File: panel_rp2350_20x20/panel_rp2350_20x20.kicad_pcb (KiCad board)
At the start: 6 copper layers, 45 x 45 mm, 548 parts, among them J1 Conn_01x04, J2 Conn_01x05, J3 Conn_01x05, J4 Conn_01x05, J5 Conn_01x05, SW1 SW_Push, SW2 SW_Push, U1 APS6404L-3SQR, U10 UCC27517, U11 UCC27517, U12 UCC27517, U13 UCC27517, U14 UCC27517, U15 UCC27517, U16 UCC27517, U17 UCC27517, U18 UCC27517, U19 UCC27517, U2 RP2354B_80QFN, U20 UCC27517, U21 UCC27517, U22 UCC27517, U23 UCC27517, U24 UCC27517, U25 UCC27517, U26 UCC27517, U27 UCC27517, U28 UCC27517, U29 UCC27517, U3 UCC27517, U30 UCC27517, U31 UCC27517, U32 UCC27517, U33 UCC27517, U34 UCC27517, U35 UCC27517, U36 UCC27517, U37 UCC27517, U38 UCC27517, U39 UCC27517, U4 UCC27517, U40 UCC27517, U41 UCC27517, U42 UCC27517, U43 AP2112K-3.3, U5 UCC27517, U6 UCC27517, U7 UCC27517, U8 UCC27517, U9 UCC27517, Y1 ABM8-272-T3

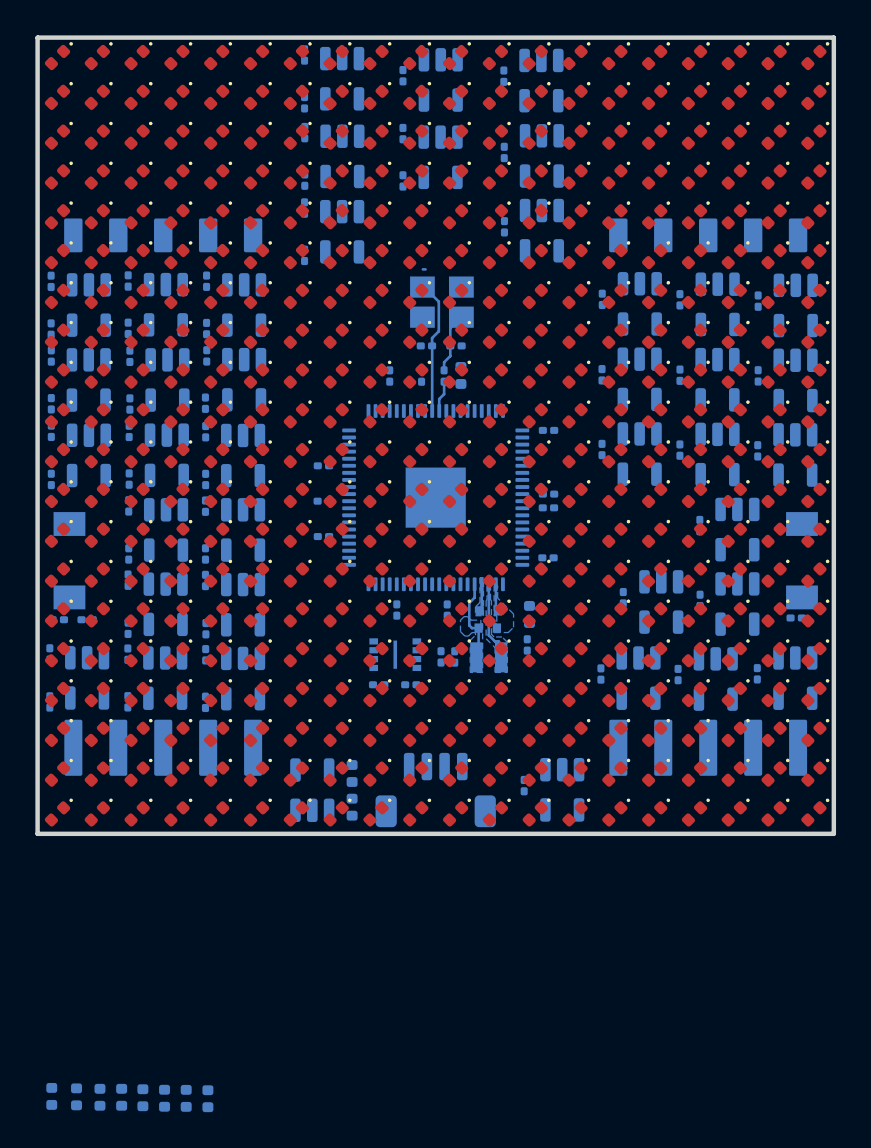
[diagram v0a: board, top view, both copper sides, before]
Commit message: Work on layout for rp2350 20x20 array panels.
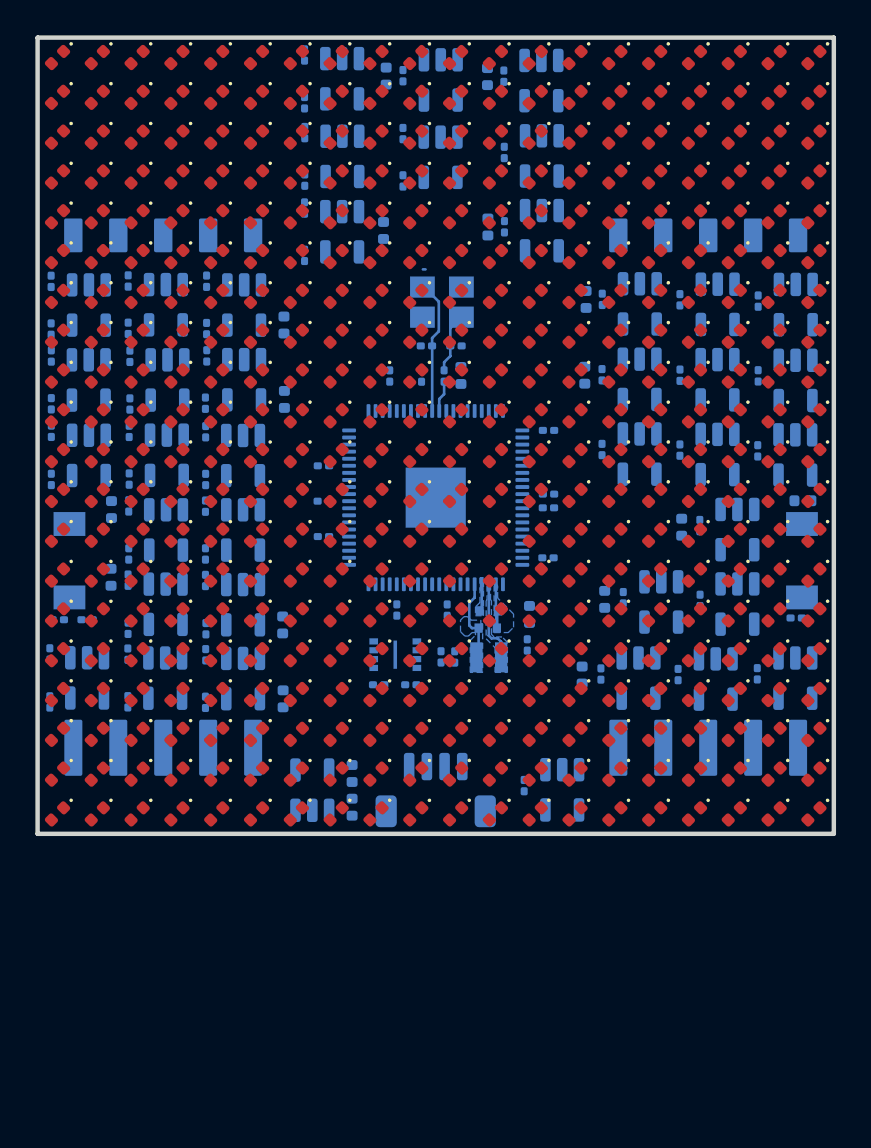
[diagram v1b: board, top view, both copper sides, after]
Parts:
- added C69: 10uF, Capacitor_SMD:C_0402_1005Metric, B.Cu at (69.7, 52.2)
- added C70: 10uF, Capacitor_SMD:C_0402_1005Metric, B.Cu at (75.4, 52.2)
- added C71: 10uF, Capacitor_SMD:C_0402_1005Metric, B.Cu at (80.9, 69.1)
- added C72: 10uF, Capacitor_SMD:C_0402_1005Metric, B.Cu at (81.0, 64.8)
- added C73: 10uF, Capacitor_SMD:C_0402_1005Metric, B.Cu at (75.5, 60.7)
- added C74: 10uF, Capacitor_SMD:C_0402_1005Metric, B.Cu at (63.9, 66.2)
- added C75: 10uF, Capacitor_SMD:C_0402_1005Metric, B.Cu at (64.0, 70.5)
- added C76: 10uF, Capacitor_SMD:C_0402_1005Metric, B.Cu at (93.3, 76.2)
- moved C60 51.2 mm to (69.5, 60.9)
- moved C63 42.7 mm to (86.4, 77.7)
- moved C61 38.4 mm to (82.0, 81.8)
- moved C59 33.2 mm to (54.2, 76.7)
- moved C65 31.9 mm to (80.8, 86.0)
- moved C64 29.7 mm to (63.9, 83.2)
- moved C62 29.6 mm to (54.1, 80.5)
- moved C66 25.3 mm to (63.9, 87.4)

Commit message: Worked on layout and routing for  rp2350 20x20 array panel.
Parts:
- D1: value LED -> LED_T0
- moved C12 0.47 mm to (69.9, 69.6)
- moved C1 0.17 mm to (72.0, 67.6)
- moved C2 0.17 mm to (73.6, 67.6)
- turned R7 to 90 degrees
- turned R8 to 90 degrees
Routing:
- net +3V3: track 1.55 -> 13.5 mm, vias 0 -> 7
- net GND: track 1.58 -> 9.86 mm, vias 0 -> 26
- net /panel_mcu/D-: track 0.00 -> 6.07 mm
- net /panel_mcu/D+: track 0.00 -> 5.96 mm
- net Net-(U2-USB_DP): track 0.00 -> 4.24 mm
- net Net-(U2-USB_DM): track 0.00 -> 4.09 mm
- net +5V: track 0.00 -> 4.02 mm, vias 0 -> 7
- net +1V1: track 4.74 -> 7.91 mm
- net /panel_mcu/VREG_AVDD: track 0.00 -> 0.98 mm
- added copper zone on In2.Cu, net +3V3
- added copper zone on In3.Cu, net +5V
- added copper zone on In1.Cu, net GND

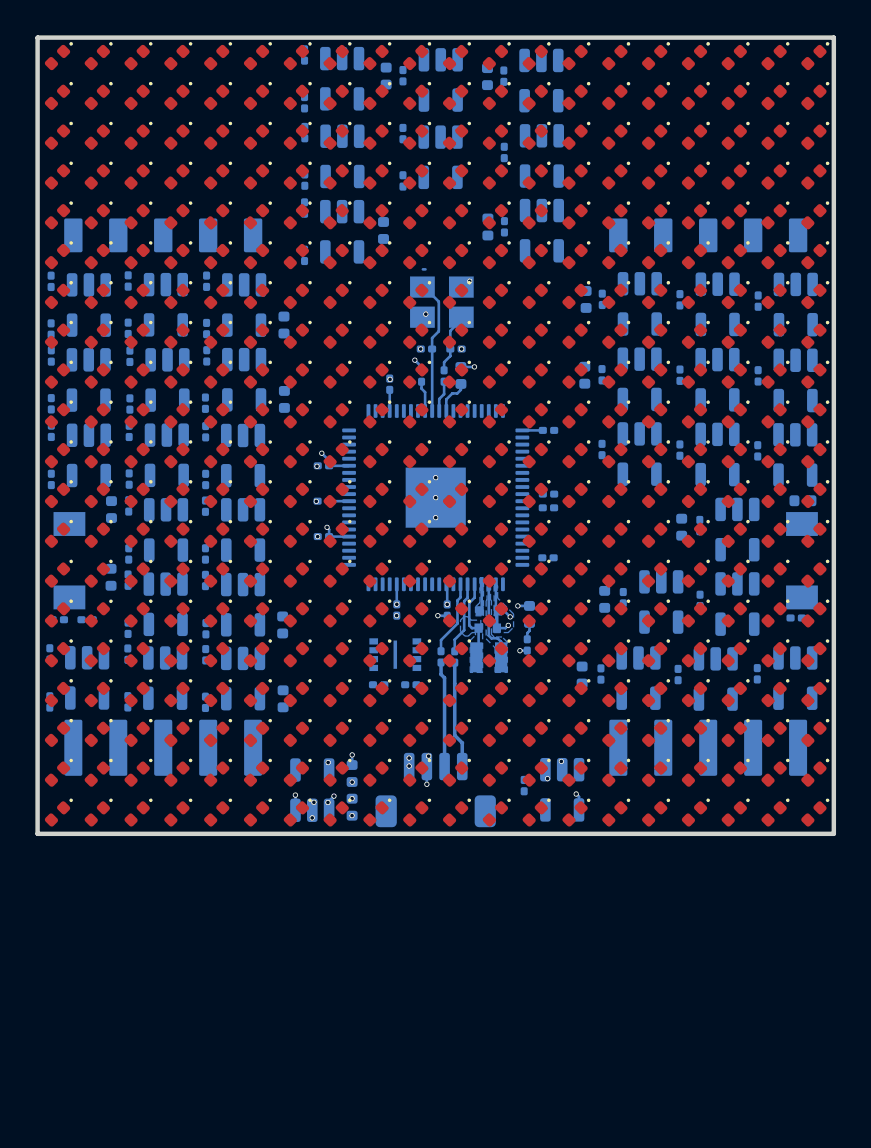
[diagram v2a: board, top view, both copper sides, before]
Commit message: Worked on rp2350 20x20 panel layout and routing.
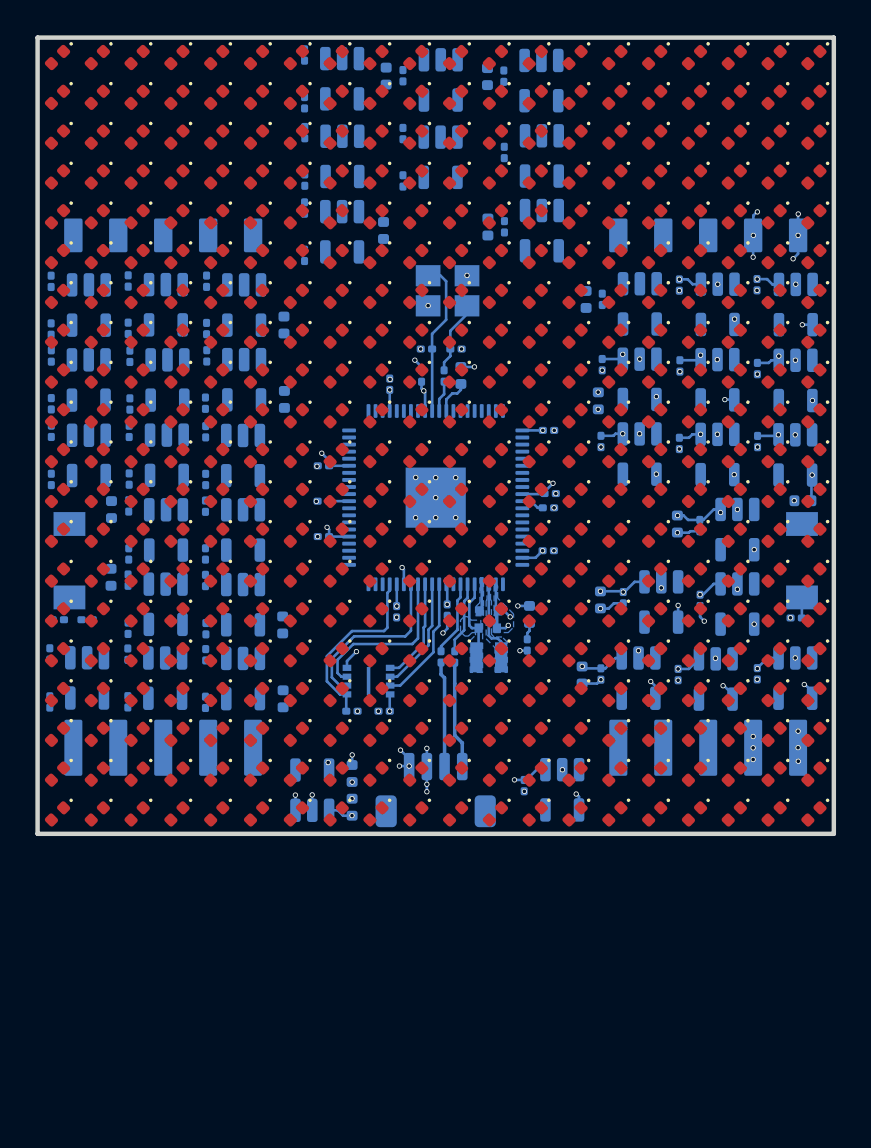
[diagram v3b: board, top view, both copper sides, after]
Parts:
- moved U1 2.12 mm to (68.7, 86.4)
- moved C3 2.12 mm to (69.6, 88.1)
- moved R1 2.12 mm to (67.8, 88.1)
- moved C71 1.64 mm to (81.7, 70.5)
- moved C47 0.93 mm to (90.7, 64.0)
- moved C42 0.83 mm to (86.3, 64.0)
- moved Y1 0.72 mm to (73.2, 64.3)
- moved C46 0.57 mm to (81.9, 68.5)
- moved C52 0.53 mm to (90.7, 72.8)
- moved C45 0.53 mm to (86.3, 68.6)
- moved C49 0.46 mm to (81.8, 72.8)
- moved C50 0.41 mm to (90.7, 68.7)
- moved C16 0.40 mm to (78.9, 79.0)
- moved C48 0.38 mm to (86.3, 72.9)
- moved C63 0.30 mm to (86.2, 77.5)
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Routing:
- net +5V: track 4.02 -> 36.3 mm, vias 7 -> 30
- net GND: track 9.86 -> 29.0 mm, vias 26 -> 87
- net /panel_mcu/XIP_CS1n: track 0.00 -> 10.4 mm
- net /panel_mcu/QSPI_SD1: track 0.00 -> 9.86 mm
- net /panel_mcu/QSPI_SD2: track 0.00 -> 9.47 mm
- net /panel_mcu/QSPI_SD3: track 0.00 -> 7.20 mm
- net /panel_mcu/QSPI_SCLK: track 0.00 -> 6.44 mm
- net /panel_mcu/QSPI_SD0: track 0.00 -> 5.84 mm
- net +3V3: track 13.5 -> 17.9 mm, vias 7 -> 14
- net +1V1: track 7.91 -> 9.22 mm
- net Net-(R2-Pad1): track 0.00 -> 1.16 mm
- net /panel_mcu/XIN: track 7.77 -> 8.83 mm
- net /panel_mcu/QSPI_SS: track 0.00 -> 0.99 mm, vias 0 -> 1
- net Net-(C2-Pad1): track 3.41 -> 4.18 mm

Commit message: Worked on rp2350 20x20 panel routing.
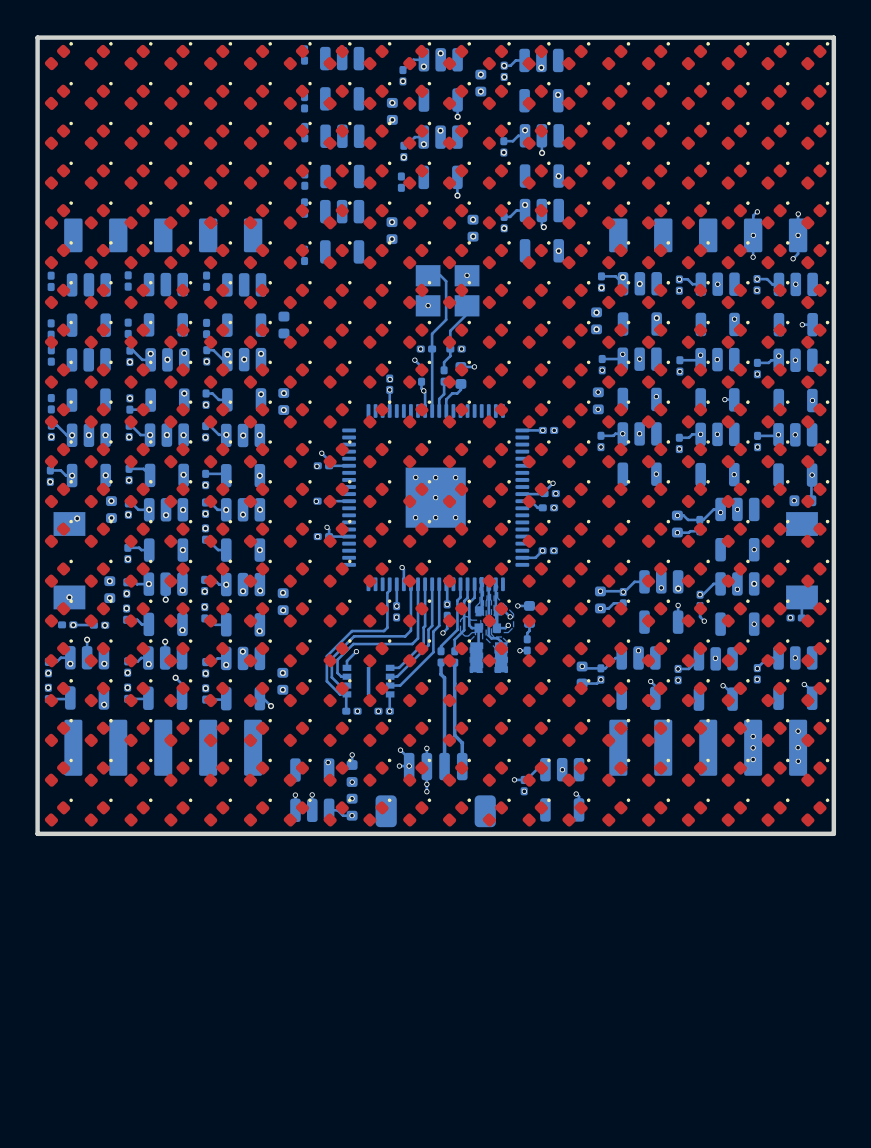
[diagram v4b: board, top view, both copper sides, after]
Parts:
- moved C69 2.03 mm to (70.0, 54.2)
- moved C72 1.35 mm to (81.6, 66.0)
- moved C64 1.32 mm to (63.9, 81.9)
- moved R14 1.13 mm to (59.5, 78.1)
- moved C38 1.01 mm to (70.7, 56.4)
- moved C66 0.99 mm to (63.9, 86.4)
- moved C43 0.98 mm to (81.9, 63.8)
- moved R12 0.90 mm to (59.5, 82.5)
- moved C73 0.84 mm to (74.6, 60.8)
- moved R13 0.80 mm to (55.0, 82.6)
- moved C21 0.78 mm to (50.6, 85.6)
- moved R4 0.77 mm to (53.5, 83.2)
- moved C19 0.73 mm to (59.5, 85.6)
- moved C20 0.73 mm to (55.1, 85.6)
- moved C62 0.70 mm to (54.1, 81.2)
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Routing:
- net +5V: track 36.3 -> 64.1 mm, vias 30 -> 58
- net GND: track 29.0 -> 43.7 mm, vias 87 -> 152
- net /drivers/COL_11: track 0.00 -> 1.74 mm
- net /drivers/COL_05: track 0.00 -> 1.42 mm
- net /drivers/COL_04: track 0.00 -> 1.36 mm
- net /drivers/COL_03: track 0.00 -> 1.36 mm
- net /drivers/COL_09: track 0.00 -> 1.36 mm, vias 0 -> 1
- net /drivers/COL_10: track 0.00 -> 1.35 mm
- net /drivers/COL_08: track 0.00 -> 1.34 mm
- net /drivers/COL_02: track 0.00 -> 1.26 mm
- net /drivers/COL_06: track 0.00 -> 1.26 mm
- net /drivers/COL_07: track 0.00 -> 1.21 mm
- net /drivers/COL_01: track 0.00 -> 1.19 mm
- net /drivers/COL_00: track 0.00 -> 1.18 mm
- net /panel_mcu/QSPI_SS: track 0.99 -> 2.16 mm, vias 1 -> 2
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
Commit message: Finished initial manual routing for rp2350 20x20 panel.
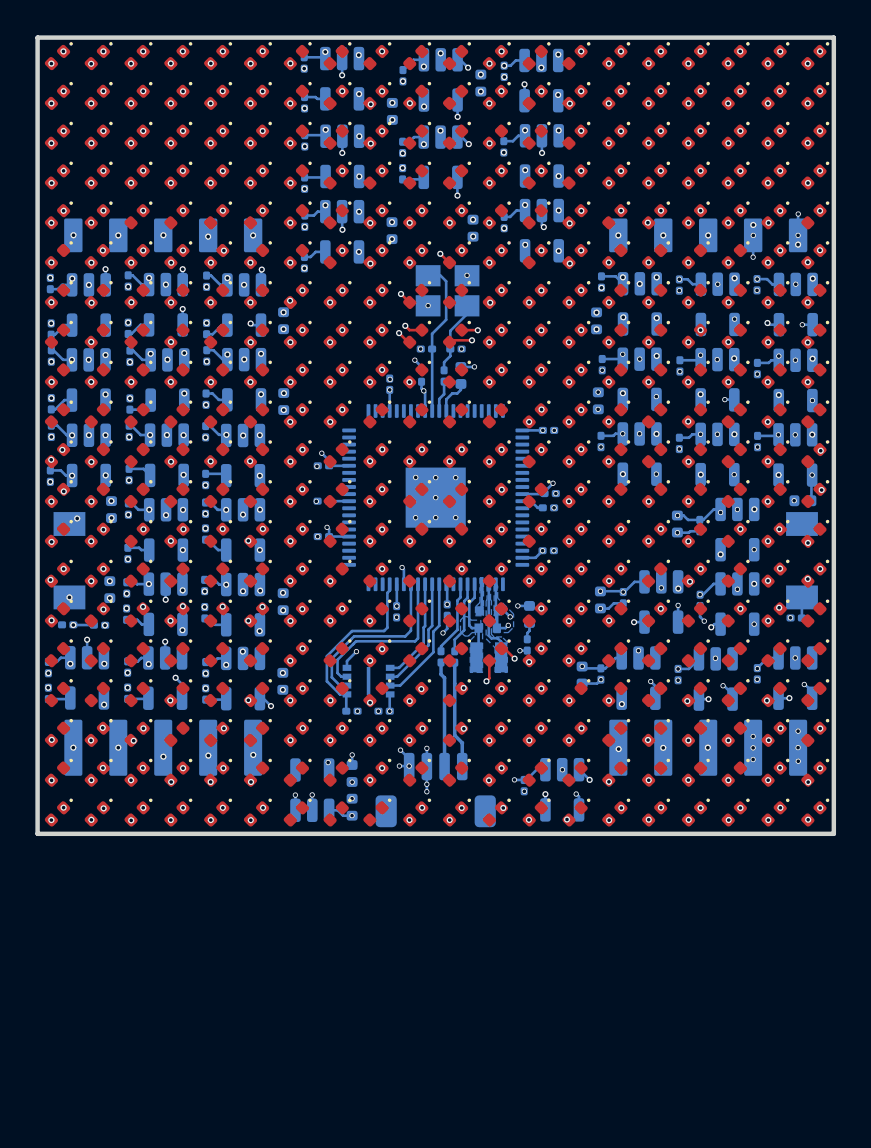
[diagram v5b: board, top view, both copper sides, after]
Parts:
- moved C34 0.74 mm to (65.1, 60.4)
- moved R28 0.48 mm to (70.6, 57.7)
- moved C33 0.47 mm to (65.1, 55.8)
- moved C37 0.45 mm to (65.1, 51.4)
- moved R24 0.41 mm to (65.1, 62.7), turned to -90 degrees
- moved C74 0.25 mm to (63.9, 66.0)
- moved C38 0.24 mm to (70.6, 56.2)
- moved R23 0.17 mm to (65.1, 58.2), turned to -90 degrees
- moved C32 0.13 mm to (50.7, 63.9), turned to 90 degrees
- turned R27 to -90 degrees
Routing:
- net +5V: track 64.1 -> 74.6 mm, vias 58 -> 66
- net GND: track 43.7 -> 48.5 mm, vias 152 -> 173
- net Net-(D201-A): track 0.01 -> 2.32 mm, vias 1 -> 10
- net Net-(D221-A): track 0.01 -> 2.14 mm, vias 1 -> 13
- net /drivers/ROW_12: track 0.00 -> 1.63 mm, vias 0 -> 9
- net /drivers/ROW_16: track 0.00 -> 1.58 mm, vias 0 -> 8
- net /drivers/COL_13: track 0.00 -> 1.41 mm
- net /drivers/ROW_03: track 0.00 -> 1.40 mm, vias 0 -> 8
- net /drivers/COL_17: track 0.00 -> 1.39 mm
- net /drivers/COL_16: track 0.00 -> 1.39 mm
- net /drivers/COL_12: track 0.00 -> 1.38 mm
- net /drivers/COL_15: track 0.00 -> 1.30 mm
- net /drivers/COL_19: track 0.00 -> 1.24 mm
- net /drivers/COL_18: track 0.00 -> 1.22 mm
- net /drivers/COL_14: track 0.00 -> 1.21 mm
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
